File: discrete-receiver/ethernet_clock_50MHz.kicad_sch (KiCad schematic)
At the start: 1 part, among them Y2 SG-5032CAN

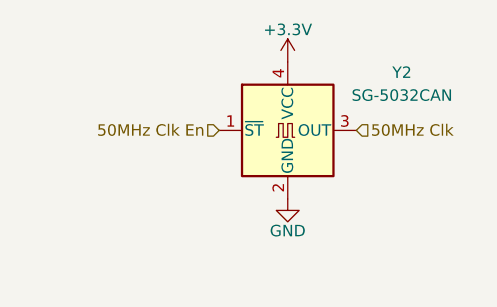
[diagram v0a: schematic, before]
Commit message: Finished Ethernet Hardware Implementation
Ethernet is now implemented using the LAN8720a IC as well as the RP2350's PIO blocks to hopefully support full speed transfer of 192kHz 24 bit stereo audio, as well as control and maybe even a web interface.
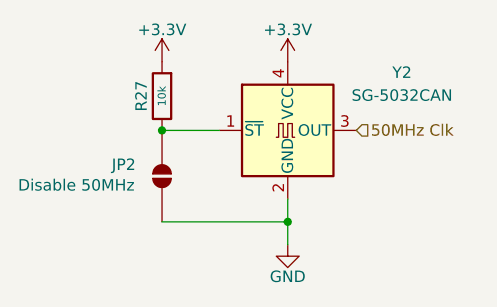
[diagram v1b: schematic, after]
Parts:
- added JP2: Disable 50MHz, symbol Jumper:SolderJumper_2_Open
- added R27: 10k, symbol Device:R
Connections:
- net +3.3V: now also R27.2
- net GND: now also JP2.2 (B)
- net 50MHz Clk En: no longer names the net of Y2.1 (~{ST})
- net 50MHz Clk En: now also JP2.1 (A), R27.1

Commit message: Organized Schematic
Standardized component labelling and font sizes. Added descriptions to some sub sheets and organized layout of root sheet.
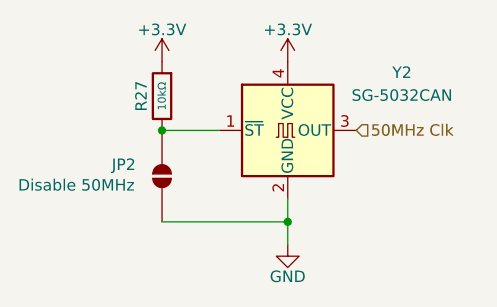
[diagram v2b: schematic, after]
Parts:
- R27: value 10k -> 10kΩ
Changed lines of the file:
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@@
 			)
 		)
-		(property "Value" "10k"
+		(property "Value" "10kΩ"
 			(at 130.81 87.63 90)
 			(show_name no)
